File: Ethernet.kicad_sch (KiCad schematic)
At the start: 1 part, among them U8 LAN8742A

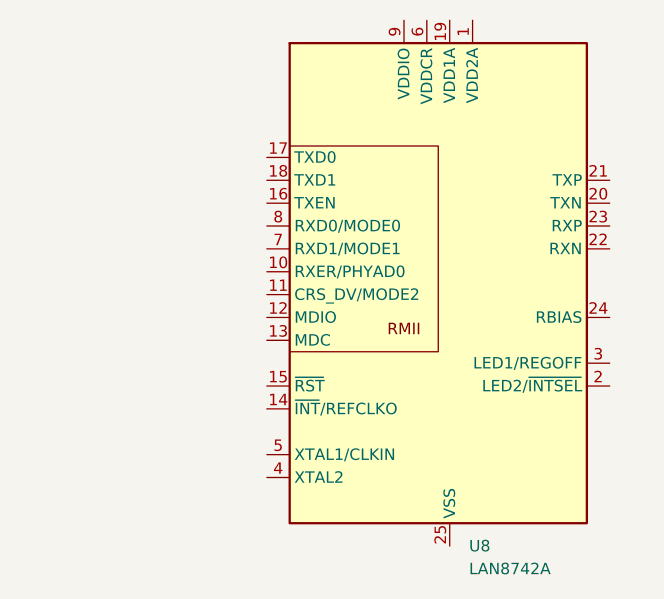
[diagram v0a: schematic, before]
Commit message: updated to use RMII and routed ethernet and CAN from micro
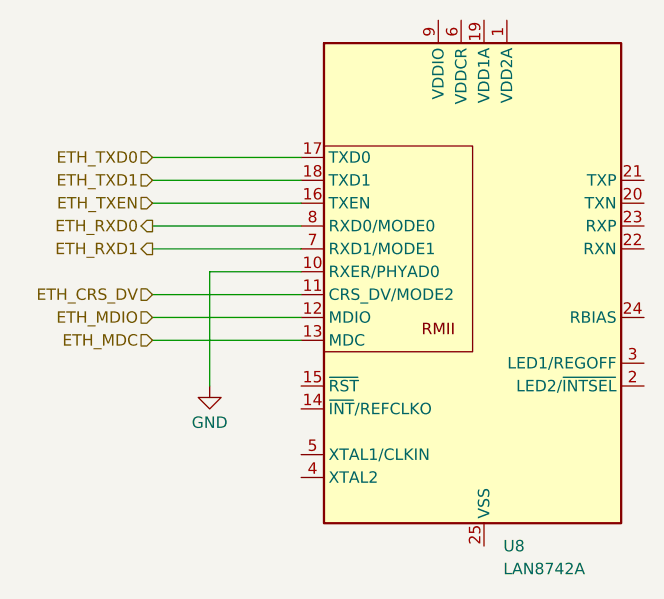
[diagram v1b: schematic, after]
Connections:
- net GND: now reaches U8.10 (RXER/PHYAD0)
- net ETH_CRS_DV: now reaches U8.11 (CRS_DV/MODE2)
- net ETH_MDIO: now reaches U8.12 (MDIO)
- net ETH_MDC: now reaches U8.13 (MDC)
- net ETH_TXEN: now reaches U8.16 (TXEN)
- net ETH_TXD0: now reaches U8.17 (TXD0)
- net ETH_TXD1: now reaches U8.18 (TXD1)
- net ETH_RXD1: now reaches U8.7 (RXD1/MODE1)
- net ETH_RXD0: now reaches U8.8 (RXD0/MODE0)
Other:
- moved on the sheet: U8
